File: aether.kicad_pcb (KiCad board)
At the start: 4 copper layers, 100.1 x 60.2 mm, 182 parts, among them J1 XT30PW-M, J2 Screw_Terminal_01x04, Q1 NPN, Q2 CSD17575Q3, Q3 CSD17575Q3, Q4 CSD17575Q3, Q5 CSD17575Q3, Q6 PNP, U1 USBLC6-2SC6, U10 TPS562201DDCR, U11 TPS562201DDCR, U12 INA219AxD, U2 USBLC6-2SC6, U3 SAM-M10Q-00B, U4 DPS310, U5 H3LIS331DL, U6 LSM6DSO32TR, U7 PCA9685PW, U8 MS860702BA01-50, U9 SHT45-AD1B-R2

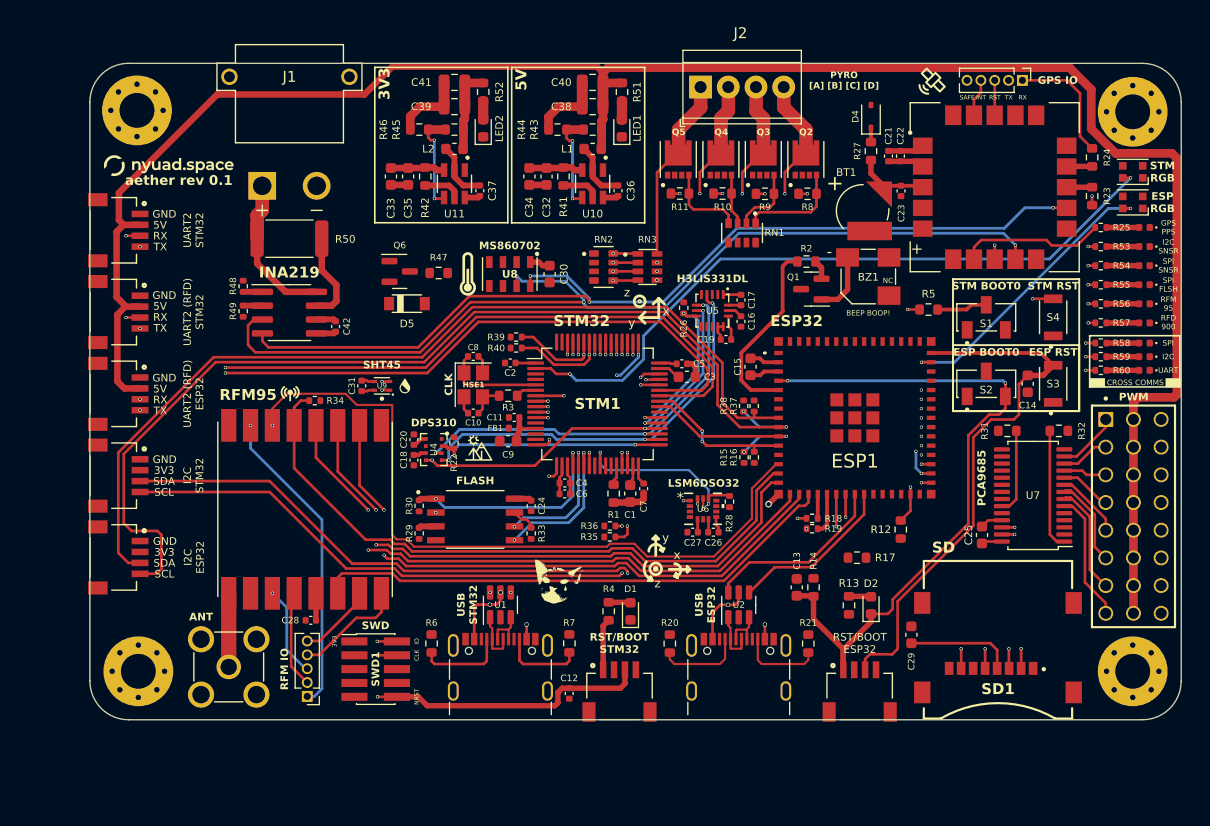
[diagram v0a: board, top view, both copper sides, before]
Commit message: updated schematics
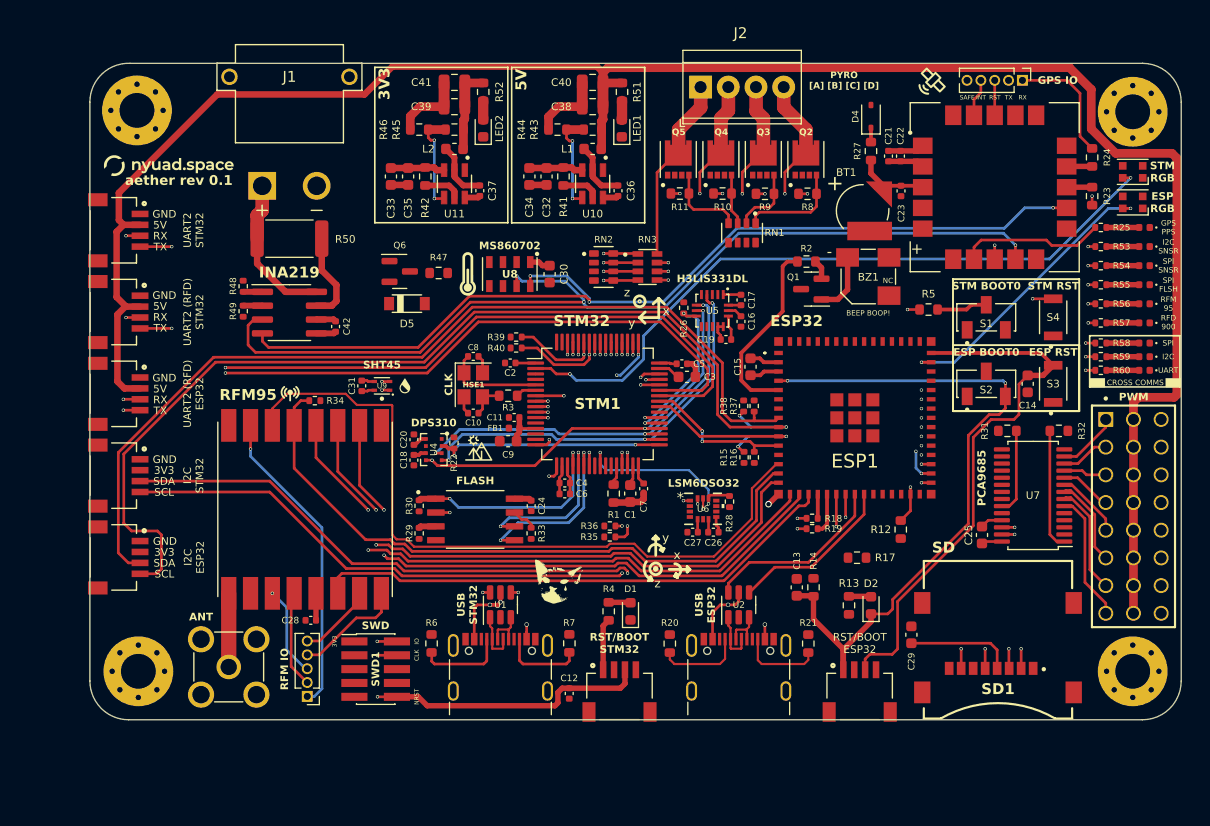
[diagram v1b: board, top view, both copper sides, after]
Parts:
- turned R37 to 90 degrees
- turned R38 to 90 degrees
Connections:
- Q2 pad 5-8: (no net) -> PYRO-TERM_D
- Q3 pad 5-8: (no net) -> PYRO-TERM_C
- Q4 pad 5-8: (no net) -> PYRO-TERM_B
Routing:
- net ESP32-TX1: track 78.2 -> 81.3 mm
- net ESP32-RX1: track 78.6 -> 81.7 mm
- net FLASH_SDI: track 13.9 -> 16.4 mm
- net FLASH_CLK: track 12.7 -> 15.3 mm
- net V-TERM_D: track 27.2 -> 28.9 mm
- net ESP32-I2C1_SCL: track 92.7 -> 94.0 mm
- net ESP32-I2C2_SDA: track 17.2 -> 18.4 mm
- net ESP32-I2C1_SDA: track 84.6 -> 85.6 mm
- net STM32_USB_D+: track 27.9 -> 28.9 mm
- net STM32_USB_D-: track 27.3 -> 28.2 mm
- net STM32-UART3_TX: track 26.2 -> 27.0 mm
- net RFM95W_RST: vias 1 -> 0

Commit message: added power planes
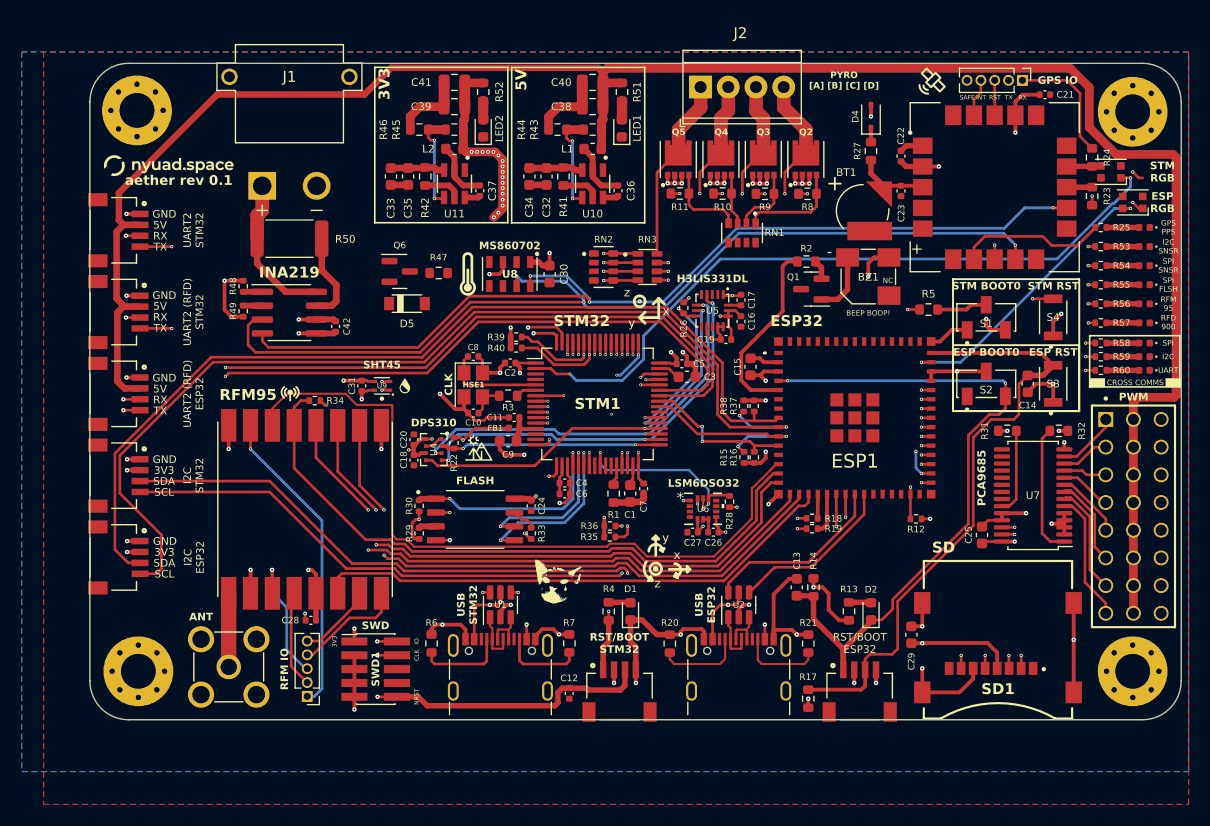
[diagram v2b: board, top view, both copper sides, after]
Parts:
- added G***: LOGO, LOGO, B.Cu at (146.0, 110.2)
- added G***: LOGO, LOGO, B.Cu at (118.0, 110.2)
- added G***: LOGO, LOGO, B.Cu at (174.0, 111.0)
- added G***: LOGO, LOGO, B.Cu at (174.1, 127.5)
- added G***: LOGO, LOGO, B.Cu at (149.9, 92.0)
- R12: footprint Resistor_SMD:R_0603_1608Metric -> Resistor_SMD:R_0402_1005Metric
- moved C21 15.4 mm to (185.8, 71.9), turned to 0 degrees
- moved R17 13.7 mm to (164.1, 127.3), turned to -90 degrees
- moved RGB1 2.00 mm to (191.9, 79.0)
- moved R12 1.71 mm to (174.0, 110.8), turned to 180 degrees
- moved D2 0.55 mm to (169.9, 119.3)
- moved R13 0.55 mm to (167.8, 119.3)
- moved C22 0.05 mm to (172.6, 77.6)
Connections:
- Q5 pad 5-8: (no net) -> PYRO-TERM_A
- REF** pad 1: (no net) -> GND (x4)
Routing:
- net GND: track 45.8 -> 188.7 mm, vias 1 -> 51
- net 3.3V: track 53.4 -> 141.4 mm, vias 0 -> 63
- net STM32-BOOT0: track 42.9 -> 69.0 mm, vias 2 -> 4
- net ESP32-EN: track 50.0 -> 56.8 mm
- net VBUS: track 43.7 -> 38.8 mm
- net RFM95W_DI3: track 8.35 -> 12.6 mm
- net DPS310_CSB: track 21.4 -> 20.2 mm
- net GPS_SCL: track 152.2 -> 153.3 mm
- net STM32-NRST: track 119.3 -> 120.3 mm
- net ESP32-I2C1_SCL: track 94.0 -> 93.0 mm
- net Net-(U7-A0): track 11.1 -> 12.0 mm
- net SPI-2_STM32: track 21.0 -> 21.9 mm
- net SPI-1_STM32: track 20.6 -> 21.5 mm
- net SPI-1_ESP32: track 20.3 -> 21.2 mm
- net RFD_900: track 19.9 -> 20.8 mm
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- added copper zone on In2.Cu, net 3.3V
- added copper zone on B.Cu, net GND
- added copper zone on F.Cu, net GND
- added copper zone on In1.Cu, net GND
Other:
- board text added: "+"
- board text added: "-"
- board text added: "@nasheed.x 26-05-2024"
- board text added: "BOOT0"
- board text added: "DI1"
- board text added: "DI2"
- board text added: "DI3"
- board text added: "DI4"
- board text added: "DI5"
- board text added: "EN"
- board text added: "GPIO0"
- board text added: "PYRO [D] [C] [B] [A]"
- board text added: "made in nyc with streetCat and"
